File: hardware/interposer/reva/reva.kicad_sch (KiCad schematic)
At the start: 28 parts, among them J1 Z80_PLUG_TO_MB, J2 5V_INPUT, U1 Z84C00_SMT44, U11 74AHCT244, U12 ESP32C3_MOD, U13 W25Q_64, U14 LDO_3V3_1A, U15 74AHCT595, U2 PICO_2, U3 74AHCT595, U4 74AHCT595, U5 74AHCT595, U6 74AHCT165, U7 74AHCT165, U8 74AHCT165, U9 74AHCT245

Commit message: hardware: fix mirrored pin placement in interposer schematic generators
The reva/rev0 generators placed a symbol pin at (x + px, y + py), but KiCad
stores symbol geometry Y-up while the sheet is Y-down, so the pin actually
lands at (x + px, y - py).  Every wire stub and net label was therefore
attached to the mirror-image pin and the netlist was broken: reva ERC
reported 93 errors (85 pin_not_connected + 8 label_dangling), rev0 58.

- reva/rev0: correct the Y transform in place(), and make Symbol.pin_pos()/
anchor() use `+hh - off` so `off` really counts down from the top of the box
  (the 'T'/'B' sides were inverted too).  Label justification flipped so the
  text runs away from the symbol body, as in the floppy-adapter generator.
- reva: the 595 drive chain is FOUR devices (U3/U4/U5/U15 -- see SR_OUT), but
  the 165 capture chain also started at y=205, putting U6 directly on top of
  U15.  That shorted SR_RCK/GND, /OE_ADDR/A0, +5V/A1, +5V/A2 and GND/A3 -- the
  netlist reported GND as "A3" with 47 nodes.  Capture chain now starts at 260.
- reva/rev0: snap symbol origins to the 1.27 mm connection grid, and size the
  Z84C00 body 111.76 mm (44 x 1.27) so its pins land on grid.  Verified
  electrically neutral: the exported netlist (nets section) is byte-identical
  with and without the snap.
- reva: fix a stale docstring that claimed to be the Rev 0 generator.

ERC: reva 93 -> 12 errors (565 -> 51 violations), rev0 58 -> 28 (286 -> 46).
The 12/28 remaining are genuinely unused pins (U7/U8 /QH, U11 2A2/2Y2, Pico
RUN/ADC_VREF/3V3_EN/VBUS, ESP32-C3 IO2/IO8/IO10), not geometry faults.  The
residual warnings are `endpoint_off_grid`-free now; what is left is
lib_symbol_issues (no 'local' entry in sym-lib-table -- the symbols are
embedded, so it is cosmetic) and isolated_pin_label on nets that are real
design gaps (/MREQ_DRV, /IORQ_RAW, /Z80_CLK, /ESP_EN, /ESP_BOOT).

Note: gen_lff_sch.py is unaffected -- it emits hierarchical sheets, no pins.

Refs #62.
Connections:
- net +3V3: now also U12.1 (3V3), U13.3 (/WP), U13.8 (VCC), U2.36 (3V3_OUT); no longer U13.1 (/CS), U13.6 (CLK), U2.25 (GP19)
- net +5V: now also J1.12 (+5V), U1.12 (+5V), U11.20 (VCC), U14.2 (VIN), U15.10 (/SCLR), U15.16 (VCC), U2.39 (VSYS), U3.10 (/SCLR), U3.16 (VCC), U4.10 (/SCLR), U4.16 (VCC), U5.10 (/SCLR), U5.16 (VCC), U6.16 (VCC), U7.16 (VCC), U8.16 (VCC), U9.20 (VCC); no longer J1.28 (/M1), J1.29 (/RFSH), J1.9 (D3), U11.13 (2A2), U11.7 (2Y2), U15.12 (RCK), U15.13 (/G), U15.7 (QH), U2.22 (GP17), U3.12 (RCK), U3.13 (/G), U3.5 (QF), U3.6 (QG), U4.12 (RCK), U4.13 (/G), U5.12 (RCK), U5.13 (/G), U6.11 (A), U6.15 (CLK_INH), U9.11 (B8)
- net /BUSAK: now also J1.24 (/BUSAK), U1.24 (/BUSAK), U2.34 (GP28); no longer J1.37 (A6), U2.27 (GP21)
- net /BUSRQ: now also J1.26 (/BUSRQ), U1.26 (/BUSRQ), U11.9 (2Y1); no longer J1.35 (A4), U11.19 (/2OE)
- net /CS_FLASH: now also U13.1 (/CS), U2.27 (GP21); no longer U13.3 (/WP), U2.34 (GP28)
- net /HALT: now also J1.19 (/HALT), U1.19 (/HALT); no longer J1.2 (A11)
- net /INT: now also J1.17 (/INT), U1.17 (/INT), U11.16 (1Y2); no longer J1.4 (A13), U11.14 (1Y3)
- net /IORQ: now also J1.21 (/IORQ), U1.21 (/IORQ); no longer J1.40 (A9)
- net /IORQ_DRV: now also U5.1 (QB); no longer U5.6 (QG)
- net /IORQ_RAW: now also U2.31 (GP26); no longer U2.30 (RUN)
- net /M1: now also J1.28 (/M1), U1.28 (/M1); no longer J1.33 (A2)
- net /M1_DRV: now also U5.4 (QE); no longer U5.3 (QD)
- net /MREQ: now also J1.20 (/MREQ), U1.20 (/MREQ); no longer J1.1 (A10)
- net /MREQ_DRV: now also U5.15 (QA); no longer U5.7 (QH)
- net /MREQ_RAW: now also U2.29 (GP22); no longer U2.32 (GP27)
- net /NMI: now also J1.18 (/NMI), U1.18 (/NMI), U11.14 (1Y3); no longer J1.3 (A12), U11.16 (1Y2)
- net /OE_ADDR: now also U15.13 (/G), U2.9 (GP6), U3.13 (/G), U4.13 (/G), U5.13 (/G); no longer J1.30 (GND), U15.10 (/SCLR), U2.12 (GP9), U3.10 (/SCLR), U3.7 (QH), U4.10 (/SCLR), U5.10 (/SCLR), U6.12 (B)
- net /OE_DATA: now also U2.7 (GP5), U9.19 (/OE); no longer U2.14 (GP10), U9.12 (B7)
- net /OE_SYSCTL: now also U11.1 (/1OE), U11.19 (/2OE), U2.10 (GP7); no longer U11.10 (GND), U11.9 (2Y1), U2.11 (GP8)
- net /RD: now also J1.22 (/RD), U1.22 (/RD); no longer J1.39 (A8)
- net /RD_DRV: now also U5.2 (QC); no longer U5.5 (QF)
- net /RESET: now also J1.27 (/RESET), U1.27 (/RESET), U11.18 (1Y1); no longer J1.34 (A3), U11.12 (1Y4)
- net /RFSH: now also J1.29 (/RFSH), U1.29 (/RFSH); no longer J1.32 (A1)
- net /RFSH_DRV: now also U5.5 (QF); no longer U5.2 (QC)
- net /WAIT: now also J1.25 (/WAIT), U1.25 (/WAIT), U11.12 (1Y4); no longer J1.36 (A5), U11.18 (1Y1)
- net /WR: now also J1.23 (/WR), U1.23 (/WR); no longer J1.38 (A7)
- net /WR_DRV: now also U5.3 (QD); no longer U5.4 (QE)
- net A10: now also J1.1 (A10), U1.1 (A10), U4.2 (QC), U7.13 (C); no longer J1.20 (/MREQ), U4.5 (QF), U7.15 (CLK_INH)
- net A11: now also J1.2 (A11), U1.2 (A11), U4.3 (QD), U7.14 (D); no longer J1.19 (/HALT), U4.4 (QE), U7.2 (CLK)
- net A12: now also J1.3 (A12), U1.3 (A12), U4.4 (QE), U7.3 (E); no longer J1.18 (/NMI), U4.3 (QD), U7.1 (SH//LD)
- net A13: now also J1.4 (A13), U1.4 (A13), U4.5 (QF), U7.4 (F); no longer J1.17 (/INT), U4.2 (QC)
- net A14: now also J1.5 (A14), U1.5 (A14), U4.6 (QG), U7.5 (G); no longer J1.16 (D1), U4.1 (QB)
- net A15: now also J1.6 (A15), U1.6 (A15), U4.7 (QH), U7.6 (H); no longer J1.15 (D0), U4.15 (QA)
- net A3: now also J1.34 (A3), U1.34 (A3), U3.3 (QD), U6.14 (D); no longer C1.2, C10.2, C11.2, C12.2, C2.2, C3.2, C4.2, C5.2, C6.2, C7.2, C8.2, C9.2, J1.27 (/RESET), J1.31 (A0), J2.2 (GND), U11.1 (/1OE), U11.11 (2A1), U11.4 (1A2), U15.11 (SCK), U15.16 (VCC), U15.3 (QD), U15.6 (QG), U2.13 (GND), U2.16 (GP12), U2.18 (GND), U2.23 (GND), U2.28 (GND), U2.3 (GND), U2.33 (GND), U2.38 (GND), U2.8 (GND), U3.11 (SCK), U3.16 (VCC), U3.4 (QE), U4.11 (SCK), U4.16 (VCC), U5.11 (SCK), U5.16 (VCC), U6.13 (C), U6.2 (CLK), U6.7 (/QH), U7.13 (C), U7.7 (/QH), U8.13 (C), U8.7 (/QH), U9.1 (DIR), U9.10 (GND)
- net A4: now also J1.35 (A4), U1.35 (A4), U3.4 (QE), U6.3 (E); no longer J1.26 (/BUSRQ), U15.14 (SER), U3.3 (QD), U6.1 (SH//LD)
- net A5: now also J1.36 (A5), U1.36 (A5), U3.5 (QF), U6.4 (F); no longer J1.25 (/WAIT), U3.2 (QC)
- net A6: now also J1.37 (A6), U1.37 (A6), U3.6 (QG), U6.5 (G); no longer J1.24 (/BUSAK), U3.1 (QB)
- net A7: now also J1.38 (A7), U1.38 (A7), U3.7 (QH), U6.6 (H); no longer J1.23 (/WR), U3.15 (QA)
- net A8: now also J1.39 (A8), U1.39 (A8), U4.15 (QA), U7.11 (A); no longer J1.22 (/RD), U4.7 (QH), U7.12 (B)
- net A9: now also J1.40 (A9), U1.40 (A9), U4.1 (QB), U7.12 (B); no longer J1.21 (/IORQ), U4.6 (QG), U7.11 (A)
- net CLK: now also J1.7 (CLK), U1.7 (CLK); no longer J1.14 (D7)
- net D0: now also J1.15 (D0), U1.15 (D0), U8.11 (A), U9.18 (B1); no longer J1.6 (A15), U8.12 (B), U9.13 (B6)
- net D1: now also J1.16 (D1), U1.16 (D1), U8.12 (B), U9.17 (B2); no longer J1.5 (A14), U8.11 (A), U9.14 (B5)
- net D2: now also J1.13 (D2), U1.13 (D2), U8.13 (C), U9.16 (B3); no longer J1.8 (D4), U8.15 (CLK_INH), U9.15 (B4)
- net D3: now also J1.9 (D3), U1.9 (D3), U8.14 (D), U9.15 (B4); no longer J1.12 (+5V), U8.2 (CLK), U9.16 (B3)
- net D4: now also J1.8 (D4), U1.8 (D4), U8.3 (E), U9.14 (B5); no longer J1.13 (D2), U8.1 (SH//LD), U9.17 (B2)
- net D5: now also J1.10 (D5), U1.10 (D5), U8.4 (F), U9.13 (B6); no longer J1.11 (D6), U9.18 (B1)
- net D6: now also J1.11 (D6), U1.11 (D6), U8.5 (G), U9.12 (B7); no longer J1.10 (D5), U9.19 (/OE)
- net D7: now also J1.14 (D7), U1.14 (D7), U8.6 (H), U9.11 (B8); no longer J1.7 (CLK), U9.20 (VCC)
- net D_/NMI: now also U11.6 (1A3), U15.2 (QC); no longer U11.8 (1A4), U15.5 (QF)
- net D_/WAIT: now also U11.8 (1A4), U15.3 (QD); no longer U11.6 (1A3), U15.4 (QE), U6.8 (GND)
- net ESP_BOOT: now also U12.3 (IO9_BOOT)
- net ESP_EN: now also U12.2 (EN)
- net ESP_RXD: now also U12.5 (TXD0), U2.22 (GP17); no longer U12.4 (RXD0), U2.39 (VSYS)
- net ESP_TXD: now also U12.4 (RXD0), U2.21 (GP16); no longer U12.5 (TXD0), U2.40 (VBUS)
- net FLASH_MISO: now also U2.26 (GP20); no longer U2.35 (ADC_VREF)
- net FLASH_MOSI: now also U13.5 (DI_MOSI), U2.25 (GP19); no longer U2.36 (3V3_OUT)
- net FLASH_SCK: now also U13.6 (CLK), U2.24 (GP18); no longer U13.8 (VCC), U2.37 (3V3_EN)
- net NC: now also U1.41 (NC), U1.42 (NC), U1.43 (NC), U1.44 (NC), U15.5 (QF), U15.6 (QG), U15.7 (QH), U15.9 (QH_), U5.6 (QG), U5.7 (QH); no longer U15.1 (QB), U15.15 (QA), U15.2 (QC), U5.1 (QB), U5.15 (QA), U6.10 (SER), U6.16 (VCC), U6.9 (QH)
- net PD0: now also U2.11 (GP8), U9.2 (A1); no longer U2.10 (GP7), U9.9 (A8)
- net PD1: now also U2.12 (GP9), U9.3 (A2); no longer U2.9 (GP6), U9.8 (A7)
- net PD2: now also U2.14 (GP10), U9.4 (A3); no longer U2.7 (GP5), U9.7 (A6)
- net PD3: now also U2.15 (GP11), U9.5 (A4); no longer U2.6 (GP4), U9.6 (A5)
- net PD4: now also U2.16 (GP12), U9.6 (A5); no longer U2.5 (GP3), U9.5 (A4)
- net PD5: now also U2.17 (GP13), U9.7 (A6); no longer U2.4 (GP2), U9.4 (A3)
- net PD6: now also U2.19 (GP14), U9.8 (A7); no longer U2.2 (GP1), U9.3 (A2)
- net PD7: now also U2.20 (GP15), U9.9 (A8); no longer U2.1 (GP0), U9.2 (A1)
- net QH_U3: now also U3.9 (QH_), U4.14 (SER)
- net QH_U4: now also U4.9 (QH_), U5.14 (SER)
- net QH_U5: now also U15.14 (SER), U5.9 (QH_); no longer U2.15 (GP11), U6.3 (E), U7.3 (E), U8.3 (E)
- net QH_U7: now also U7.9 (QH), U8.10 (SER)
- net SR_MISO: now also U2.4 (GP2), U8.9 (QH); no longer U2.17 (GP13)
- net SR_MOSI: now also U2.2 (GP1), U3.14 (SER); no longer U2.19 (GP14)
- net SR_SCK: now also U15.11 (SCK), U2.1 (GP0), U3.11 (SCK), U4.11 (SCK), U5.11 (SCK), U6.2 (CLK), U7.2 (CLK), U8.2 (CLK); no longer U15.8 (GND), U2.20 (GP15), U3.8 (GND), U4.8 (GND), U5.8 (GND), U6.14 (D), U7.14 (D), U8.14 (D)
- net Z80_CLK: now also U2.32 (GP27); no longer U2.29 (GP22)
- net GND: now reaches U12.10 (GND)
- net GND: now also C1.2, C10.2, C11.2, C12.2, C2.2, C3.2, C4.2, C5.2, C6.2, C7.2, C8.2, C9.2, J1.30 (GND), J2.2 (GND), U1.30 (GND), U11.10 (GND), U13.4 (GND), U14.1 (GND), U15.8 (GND), U2.13 (GND), U2.18 (GND), U2.23 (GND), U2.28 (GND), U2.3 (GND), U2.33 (GND), U2.38 (GND), U2.8 (GND), U3.8 (GND), U4.8 (GND), U5.8 (GND), U6.10 (SER), U6.15 (CLK_INH), U6.8 (GND), U7.15 (CLK_INH), U7.8 (GND), U8.15 (CLK_INH), U8.8 (GND), U9.1 (DIR), U9.10 (GND)
- net A0: now reaches U1.31 (A0)
- net A0: now also J1.31 (A0), U3.15 (QA), U6.11 (A)
- net A1: now reaches U1.32 (A1)
- net A1: now also J1.32 (A1), U3.1 (QB), U6.12 (B)
- net A2: now reaches U1.33 (A2)
- net A2: now also J1.33 (A2), U3.2 (QC), U6.13 (C)
- net D_/RESET: now reaches U11.2 (1A1)
- net D_/RESET: now also U15.15 (QA)
- net QH_U6: now reaches U7.10 (SER)
- net QH_U6: now also U6.9 (QH)
- new net D_/BUSRQ: U11.11 (2A1), U15.4 (QE)
- new net D_/INT: U11.4 (1A2), U15.1 (QB)
- new net SR_LOAD: U2.6 (GP4), U6.1 (SH//LD), U7.1 (SH//LD), U8.1 (SH//LD)
- new net SR_RCK: U15.12 (RCK), U2.5 (GP3), U3.12 (RCK), U4.12 (RCK), U5.12 (RCK)

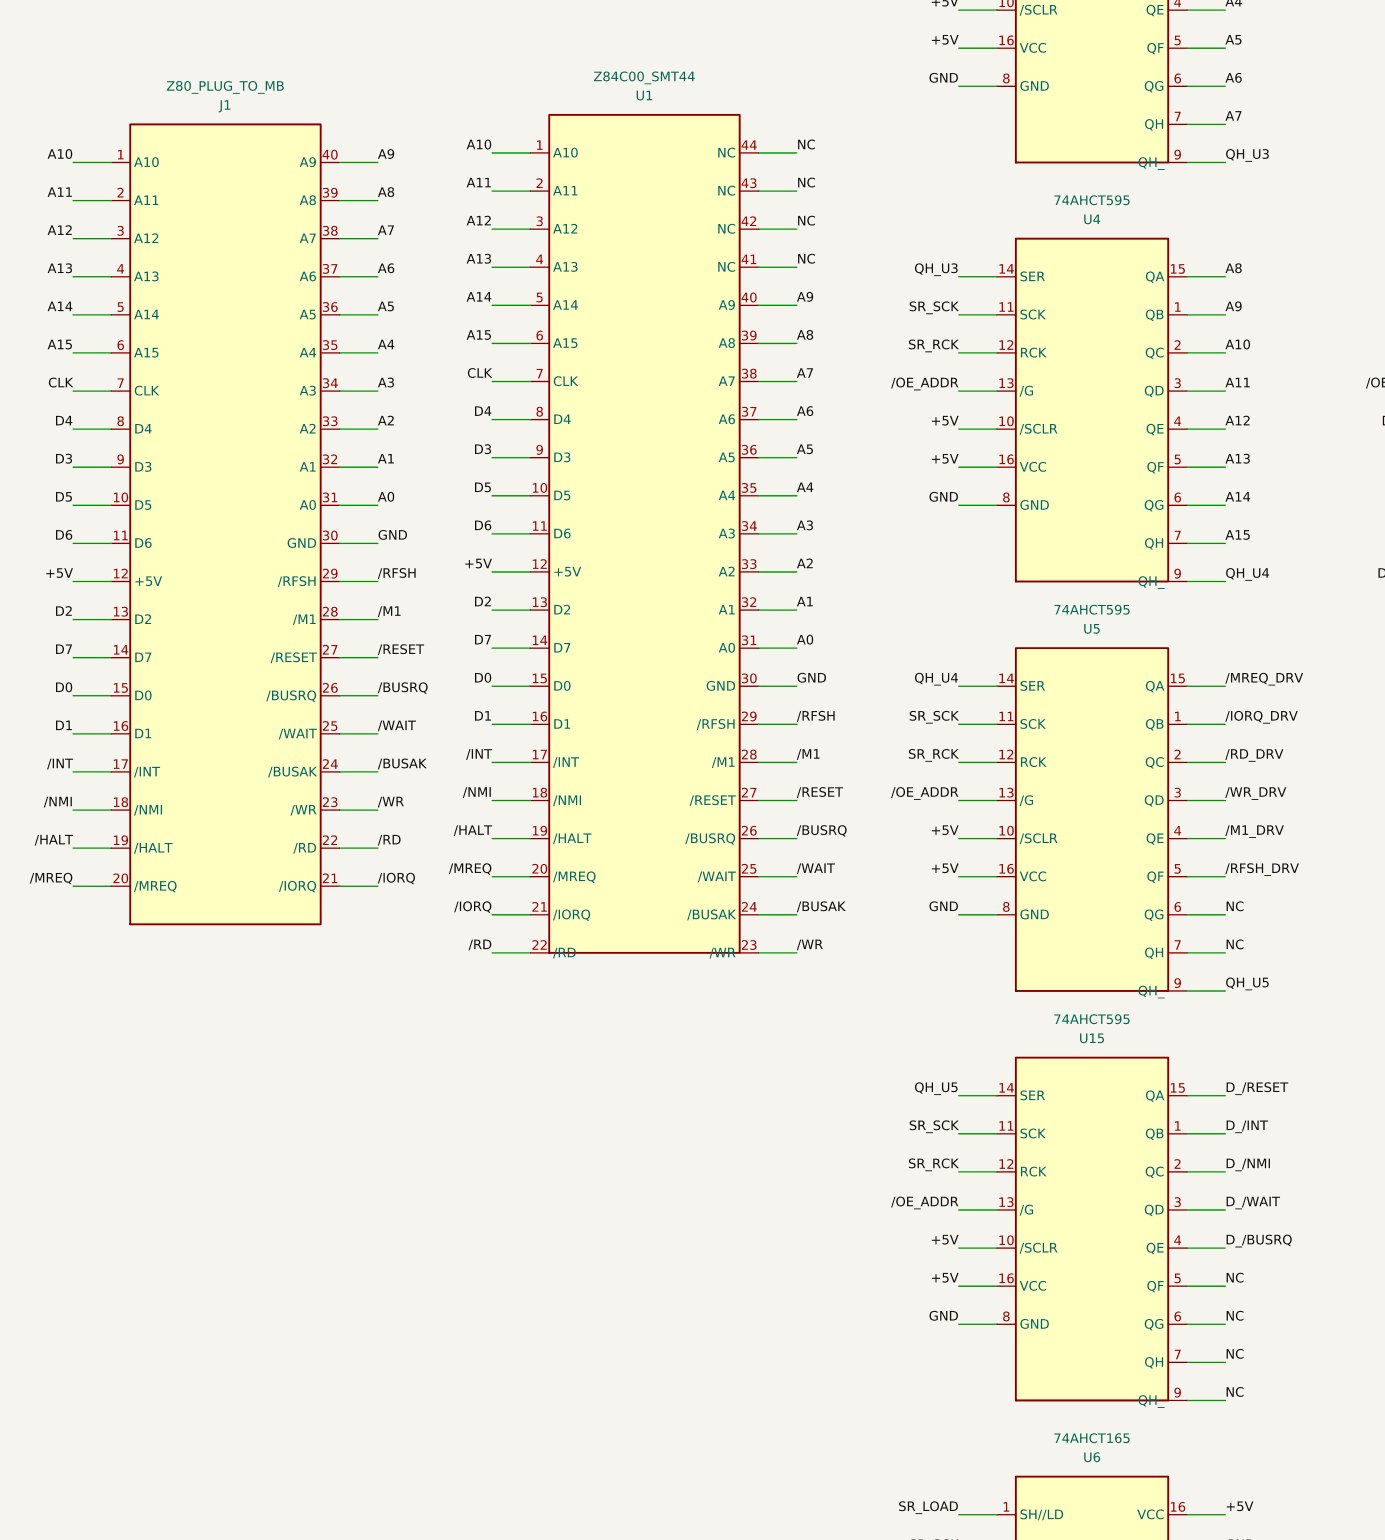
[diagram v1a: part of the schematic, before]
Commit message: hardware: correct the Z80 DIP-40 pinout in the interposer generators (#62)
Both generators carried a Z80 pin table shifted by one pin: pin 1 = A10,
pin 11 = D6, pin 12 = +5V, pin 30 = GND, pin 31 = A0.  The real Zilog DIP-40 is
pin 1 = A11, pin 11 = +5V, pin 29 = GND, pin 30 = A0 (Z80 Microprocessor Family
Databook, cross-checked against z80.info/zinout.htm).  Because J1 plugs into the
O1's Z80 socket and J2/U1 mate with the CPU, every address, data and control
line was tapped one pin off -- the netlist put +5V on the D2 net and shorted
A0 to GND, which would have damaged a real board.

- reva/rev0: define the pinout once (Z80_LEFT/Z80_RIGHT) and derive both the
  symbol geometry and Z80NET from it, reva's Z84C00 symbol included.  Keeping
  two hand-written copies is how the off-by-one survived.
- reva/rev0: 'NC' was used as a net *label*, which ties every unused pin onto
  one net -- on reva that joined four unused 74AHCT595 totem-pole outputs
  (output contention) plus the Z84C00's four NC pins.  Unused pins now get real
  no-connect flags.
- docs/o1-memory-io-map.md sec.6: the Z80 table there was wrong too (it claimed
  pin 11 = GND).  Replaced with the datasheet pinout.
- docs/research-gaps.md gap #3: Z80 half resolved; the char-gen socket pinout
  is still open for the ScreenPac personality (#24).

Reva ERC stays at 12 errors (all genuinely unused pins).  The netlist now reads
correctly: GND = 40 nodes, A0 = J1.30/U1.30/U3.15/U6.11.

part of #62
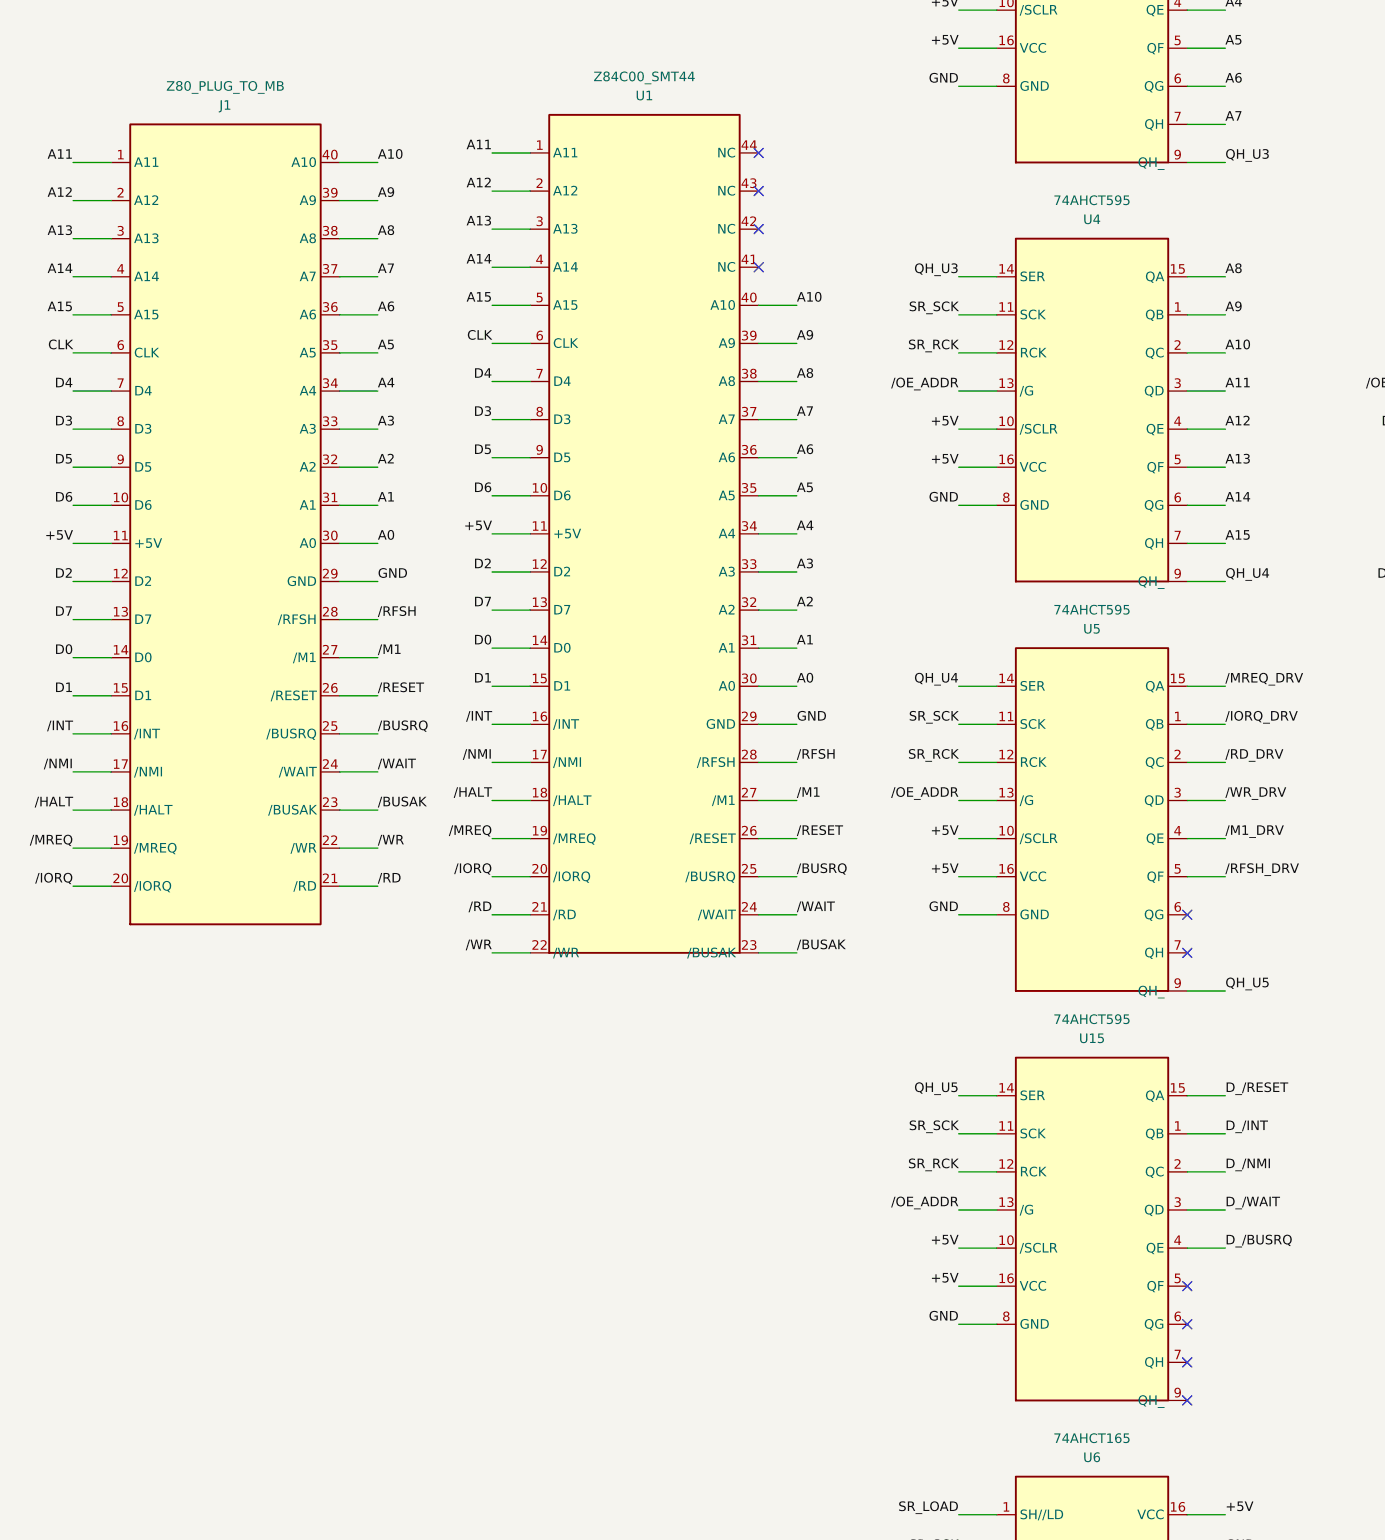
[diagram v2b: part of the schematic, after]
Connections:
- net +5V: now also J1.11 (+5V), U1.11 (+5V); no longer J1.12 (+5V), U1.12 (+5V)
- net /BUSAK: now also J1.23 (/BUSAK), U1.23 (/BUSAK); no longer J1.24 (/BUSAK), U1.24 (/BUSAK)
- net /BUSRQ: now also J1.25 (/BUSRQ), U1.25 (/BUSRQ); no longer J1.26 (/BUSRQ), U1.26 (/BUSRQ)
- net /HALT: now also J1.18 (/HALT), U1.18 (/HALT); no longer J1.19 (/HALT), U1.19 (/HALT)
- net /INT: now also J1.16 (/INT), U1.16 (/INT); no longer J1.17 (/INT), U1.17 (/INT)
- net /IORQ: now also J1.20 (/IORQ), U1.20 (/IORQ); no longer J1.21 (/IORQ), U1.21 (/IORQ)
- net /M1: now also J1.27 (/M1), U1.27 (/M1); no longer J1.28 (/M1), U1.28 (/M1)
- net /MREQ: now also J1.19 (/MREQ), U1.19 (/MREQ); no longer J1.20 (/MREQ), U1.20 (/MREQ)
- net /NMI: now also J1.17 (/NMI), U1.17 (/NMI); no longer J1.18 (/NMI), U1.18 (/NMI)
- net /RD: now also J1.21 (/RD), U1.21 (/RD); no longer J1.22 (/RD), U1.22 (/RD)
- net /RESET: now also J1.26 (/RESET), U1.26 (/RESET); no longer J1.27 (/RESET), U1.27 (/RESET)
- net /RFSH: now also J1.28 (/RFSH), U1.28 (/RFSH); no longer J1.29 (/RFSH), U1.29 (/RFSH)
- net /WAIT: now also J1.24 (/WAIT), U1.24 (/WAIT); no longer J1.25 (/WAIT), U1.25 (/WAIT)
- net /WR: now also J1.22 (/WR), U1.22 (/WR); no longer J1.23 (/WR), U1.23 (/WR)
- net A0: now also J1.30 (A0), U1.30 (A0); no longer J1.31 (A0), U1.31 (A0)
- net A1: now also J1.31 (A1), U1.31 (A1); no longer J1.32 (A1), U1.32 (A1)
- net A10: now also J1.40 (A10), U1.40 (A10); no longer J1.1 (A10), U1.1 (A10)
- net A11: now also J1.1 (A11), U1.1 (A11); no longer J1.2 (A11), U1.2 (A11)
- net A12: now also J1.2 (A12), U1.2 (A12); no longer J1.3 (A12), U1.3 (A12)
- net A13: now also J1.3 (A13), U1.3 (A13); no longer J1.4 (A13), U1.4 (A13)
- net A14: now also J1.4 (A14), U1.4 (A14); no longer J1.5 (A14), U1.5 (A14)
- net A15: now also J1.5 (A15), U1.5 (A15); no longer J1.6 (A15), U1.6 (A15)
- net A2: now also J1.32 (A2), U1.32 (A2); no longer J1.33 (A2), U1.33 (A2)
- net A3: now also J1.33 (A3), U1.33 (A3); no longer J1.34 (A3), U1.34 (A3)
- net A4: now also J1.34 (A4), U1.34 (A4); no longer J1.35 (A4), U1.35 (A4)
- net A5: now also J1.35 (A5), U1.35 (A5); no longer J1.36 (A5), U1.36 (A5)
- net A6: now also J1.36 (A6), U1.36 (A6); no longer J1.37 (A6), U1.37 (A6)
- net A7: now also J1.37 (A7), U1.37 (A7); no longer J1.38 (A7), U1.38 (A7)
- net A8: now also J1.38 (A8), U1.38 (A8); no longer J1.39 (A8), U1.39 (A8)
- net A9: now also J1.39 (A9), U1.39 (A9); no longer J1.40 (A9), U1.40 (A9)
- net CLK: now also J1.6 (CLK), U1.6 (CLK); no longer J1.7 (CLK), U1.7 (CLK)
- net D0: now also J1.14 (D0), U1.14 (D0); no longer J1.15 (D0), U1.15 (D0)
- net D1: now also J1.15 (D1), U1.15 (D1); no longer J1.16 (D1), U1.16 (D1)
- net D2: now also J1.12 (D2), U1.12 (D2); no longer J1.13 (D2), U1.13 (D2)
- net D3: now also J1.8 (D3), U1.8 (D3); no longer J1.9 (D3), U1.9 (D3)
- net D4: now also J1.7 (D4), U1.7 (D4); no longer J1.8 (D4), U1.8 (D4)
- net D5: now also J1.9 (D5), U1.9 (D5); no longer J1.10 (D5), U1.10 (D5)
- net D6: now also J1.10 (D6), U1.10 (D6); no longer J1.11 (D6), U1.11 (D6)
- net D7: now also J1.13 (D7), U1.13 (D7); no longer J1.14 (D7), U1.14 (D7)
- net GND: now also J1.29 (GND), U1.29 (GND); no longer J1.30 (GND), U1.30 (GND)
- removed net NC: U1.41 (NC), U1.42 (NC), U1.43 (NC), U1.44 (NC), U15.5 (QF), U15.6 (QG), U15.7 (QH), U15.9 (QH_), U5.6 (QG), U5.7 (QH)
- no-connect marks 0 -> 10
